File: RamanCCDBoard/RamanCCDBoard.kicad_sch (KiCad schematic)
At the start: 8 parts, among them J1 Conn_01x03_Pin, U1 ILX511

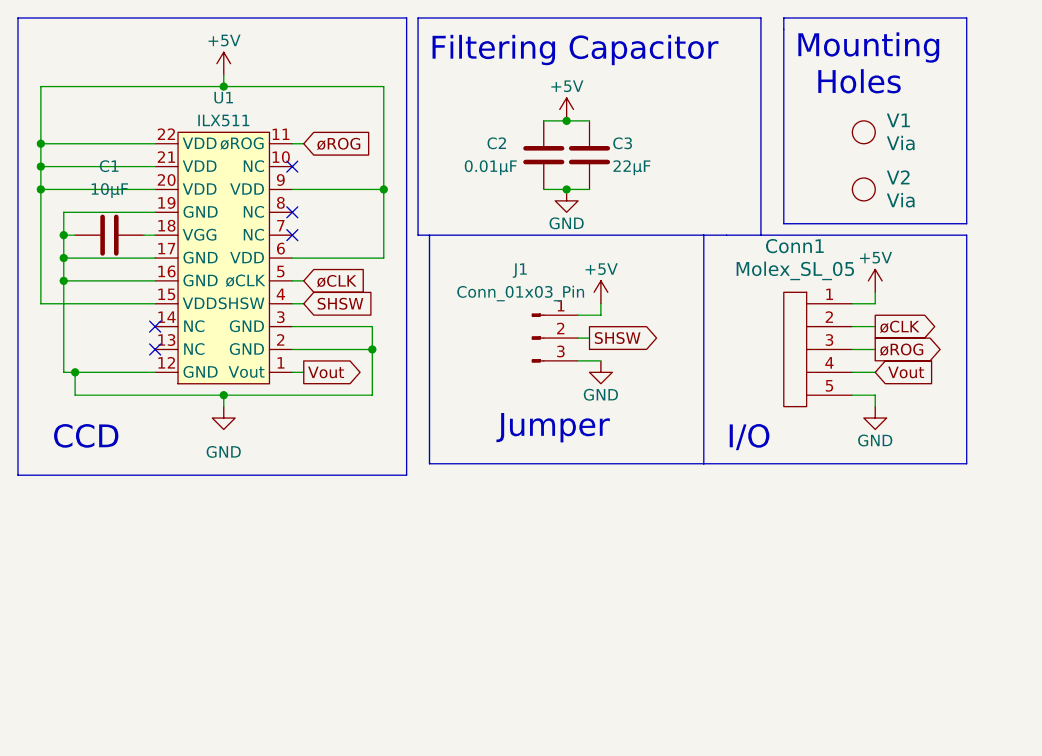
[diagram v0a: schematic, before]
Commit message: add bjt to ccd
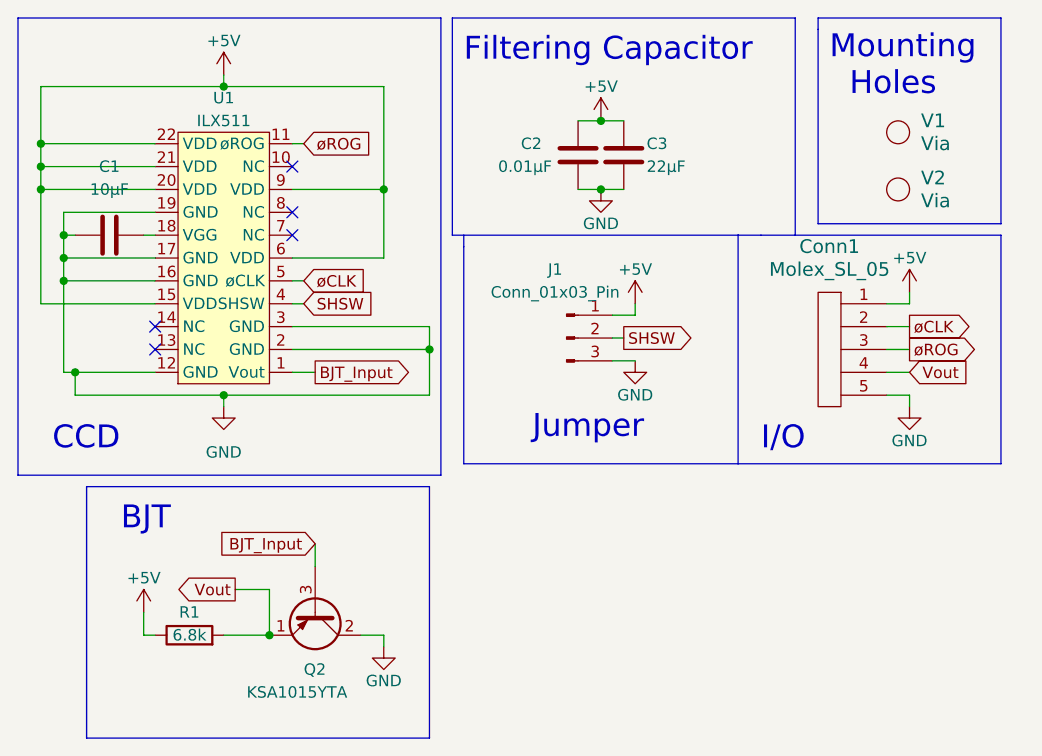
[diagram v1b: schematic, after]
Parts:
- added Q2: KSA1015YTA, Package_TO_SOT_THT:TO-92_Inline, symbol Transistor_BJT:BC636
- added R1: 6.8k, Resistor_SMD:R_0603_1608Metric_Pad0.98x0.95mm_HandSolder, symbol Device:R
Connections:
- net +5V: now also R1.1
- net GND: now also Q2.2 (C)
- net Vout: now also Q2.1 (E), R1.2; no longer U1.1 (Vout)
- new net BJT_Input: Q2.3 (B), U1.1 (Vout)
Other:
- note added: "BJT"
- moved on the sheet: C2, C3, Conn1, J1, V1, V2

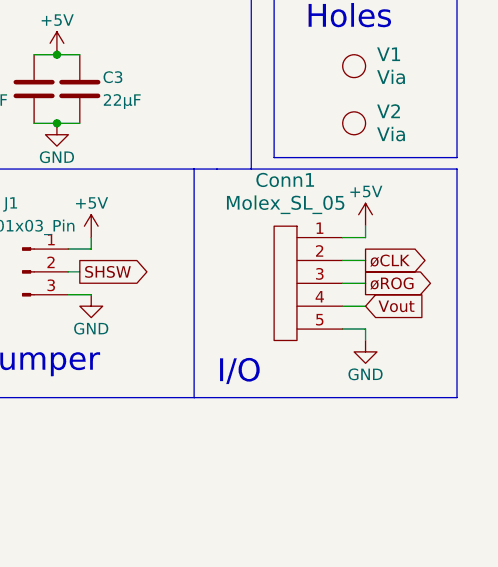
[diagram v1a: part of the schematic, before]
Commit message: change pin ordering for ccd molex
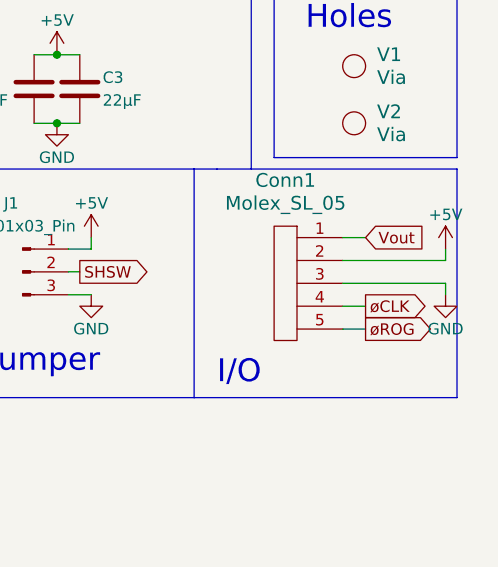
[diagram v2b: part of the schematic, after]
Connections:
- net +5V: now also Conn1.2; no longer Conn1.1
- net GND: now also Conn1.3; no longer Conn1.5
- net Vout: now also Conn1.1; no longer Conn1.4
- net øCLK: now also Conn1.4; no longer Conn1.2
- net øROG: now also Conn1.5; no longer Conn1.3
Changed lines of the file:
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@@
-    (stroke (width 0) (type default))
-  )
-  (wire (pts (xy 111.76 44.45) (xy 111.76 43.18))
     (stroke (width 0) (type default))
   )
@@
     (stroke (width 0) (type default))
   )
-  (wire (pts (xy 111.76 54.61) (xy 111.76 55.88))
+  (wire (pts (xy 120.65 50.8) (xy 120.65 49.53))
     (stroke (width 0) (type default))
   )
@@
     (stroke (width 0) (type default))
   )
-  (wire (pts (xy 109.22 49.53) (xy 111.76 49.53))
-    (stroke (width 0) (type default))
-  )
   (polyline (pts (xy 12.7 12.7) (xy 59.69 12.7))
     (stroke (width 0) (type default))
@@
     (stroke (width 0) (type default))
   )
+  (wire (pts (xy 109.22 49.53) (xy 120.65 49.53))
+    (stroke (width 0) (type default))
+  )
   (polyline (pts (xy 101.6 35.56) (xy 121.92 35.56))
     (stroke (width 0) (type default))
@@
     (stroke (width 0) (type default))
   )
-  (wire (pts (xy 109.22 46.99) (xy 111.76 46.99))
+  (wire (pts (xy 120.65 46.99) (xy 120.65 45.72))
+    (stroke (width 0) (type default))
+  )
+  (wire (pts (xy 109.22 46.99) (xy 120.65 46.99))
     (stroke (width 0) (type default))
   )
@@
     (effects (font (size 1.27 1.27)) (justify left))
     (property "Intersheetrefs" "${INTERSHEET_REFS}" (at 52.6361 44.45 0)
-      (effects (font (size 1.27 1.27)) (justify left) hide)
-    )
-  )
-  (global_label "øROG" (shape output) (at 111.76 49.53 0) (fields_autoplaced)
-    (effects (font (size 1.27 1.27)) (justify left))
-    (property "Intersheetrefs" "${INTERSHEET_REFS}" (at 119.7647 49.53 0)
       (effects (font (size 1.27 1.27)) (justify left) hide)
     )
@@
     )
   )
-  (global_label "Vout" (shape input) (at 111.76 52.07 0) (fields_autoplaced)
-    (effects (font (size 1.27 1.27)) (justify left))
-    (property "Intersheetrefs" "${INTERSHEET_REFS}" (at 118.8575 52.07 0)
-      (effects (font (size 1.27 1.27)) (justify left) hide)
-    )
-  )
   (global_label "BJT_Input" (shape input) (at 45.72 71.12 180) (fields_autoplaced)
     (effects (font (size 1.27 1.27)) (justify right))
@@
     )
   )
-  (global_label "øCLK" (shape output) (at 111.76 46.99 0) (fields_autoplaced)
-    (effects (font (size 1.27 1.27)) (justify left))
-    (property "Intersheetrefs" "${INTERSHEET_REFS}" (at 119.4623 46.99 0)
+  (global_label "Vout" (shape input) (at 111.76 44.45 0) (fields_autoplaced)
+    (effects (font (size 1.27 1.27)) (justify left))
+    (property "Intersheetrefs" "${INTERSHEET_REFS}" (at 118.8575 44.45 0)
+      (effects (font (size 1.27 1.27)) (justify left) hide)
+    )
+  )
+  (global_label "øROG" (shape output) (at 111.76 54.61 0) (fields_autoplaced)
+    (effects (font (size 1.27 1.27)) (justify left))
+    (property "Intersheetrefs" "${INTERSHEET_REFS}" (at 119.7647 54.61 0)
+      (effects (font (size 1.27 1.27)) (justify left) hide)
+    )
+  )
+  (global_label "øCLK" (shape output) (at 111.76 52.07 0) (fields_autoplaced)
+    (effects (font (size 1.27 1.27)) (justify left))
+    (property "Intersheetrefs" "${INTERSHEET_REFS}" (at 119.4623 52.07 0)
       (effects (font (size 1.27 1.27)) (justify left) hide)
     )
@@
         (path "/64b006a0-b432-4c05-bc21-eb3325874dfb"
           (reference "#PWR01") (unit 1)
-        )
-      )
-    )
-  )
-  (symbol (lib_id "power:+5V") (at 111.76 43.18 0) (unit 1)
-    (in_bom yes) (on_board yes) (dnp no)
-    (property "Reference" "#PWR08" (at 111.76 46.99 0)
-      (effects (font (size 1.27 1.27)) hide)
-    )
-    (property "Value" "+5V" (at 111.76 39.37 0)
-      (effects (font (size 1.27 1.27)))
-    )
-    (property "Footprint" "" (at 111.76 43.18 0)
-      (effects (font (size 1.27 1.27)) hide)
-    )
-    (property "Datasheet" "" (at 111.76 43.18 0)
-      (effects (font (size 1.27 1.27)) hide)
-    )
-    (pin "1")
-    (instances
-      (project "RamanCCDBoard"
-        (path "/64b006a0-b432-4c05-bc21-eb3325874dfb"
-          (reference "#PWR08") (unit 1)
         )
       )
@@
     )
   )
-  (symbol (lib_id "power:GND") (at 111.76 55.88 0) (unit 1)
-    (in_bom yes) (on_board yes) (dnp no)
-    (property "Reference" "#PWR07" (at 111.76 62.23 0)
-      (effects (font (size 1.27 1.27)) hide)
-    )
-    (property "Value" "GND" (at 111.76 59.69 0)
-      (effects (font (size 1.27 1.27)))
-    )
-    (property "Footprint" "" (at 111.76 55.88 0)
-      (effects (font (size 1.27 1.27)) hide)
-    )
-    (property "Datasheet" "" (at 111.76 55.88 0)
+  (symbol (lib_id "power:GND") (at 120.65 50.8 0) (unit 1)
+    (in_bom yes) (on_board yes) (dnp no)
+    (property "Reference" "#PWR07" (at 120.65 57.15 0)
+      (effects (font (size 1.27 1.27)) hide)
+    )
+    (property "Value" "GND" (at 120.65 54.61 0)
+      (effects (font (size 1.27 1.27)))
+    )
+    (property "Footprint" "" (at 120.65 50.8 0)
+      (effects (font (size 1.27 1.27)) hide)
+    )
+    (property "Datasheet" "" (at 120.65 50.8 0)
       (effects (font (size 1.27 1.27)) hide)
     )
@@
         )
       )
+    )
+  )
+  (symbol (lib_id "power:+5V") (at 120.65 45.72 0) (unit 1)
+    (in_bom yes) (on_board yes) (dnp no)
+    (property "Reference" "#PWR08" (at 120.65 49.53 0)
+      (effects (font (size 1.27 1.27)) hide)
+    )
+    (property "Value" "+5V" (at 120.65 41.91 0)
+      (effects (font (size 1.27 1.27)))
+    )
+    (property "Footprint" "" (at 120.65 45.72 0)
+      (effects (font (size 1.27 1.27)) hide)
+    )
+    (property "Datasheet" "" (at 120.65 45.72 0)
+      (effects (font (size 1.27 1.27)) hide)
+    )
+    (pin "1")
+    (instances
+      (project "RamanCCDBoard"
+        (path "/64b006a0-b432-4c05-bc21-eb3325874dfb"
+          (reference "#PWR08") (unit 1)
+        )
+      )
